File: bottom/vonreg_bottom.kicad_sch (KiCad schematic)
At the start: 7 parts, among them J1 AudioJack4, T1 SW_Push, T2 SW_Push, T3 SW_Push

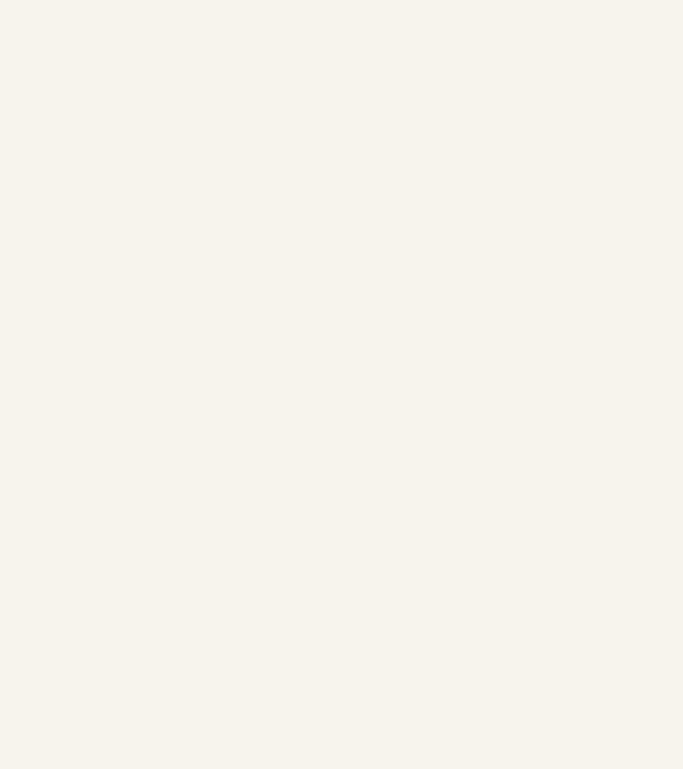
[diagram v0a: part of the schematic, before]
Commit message: Aligned top/bottom
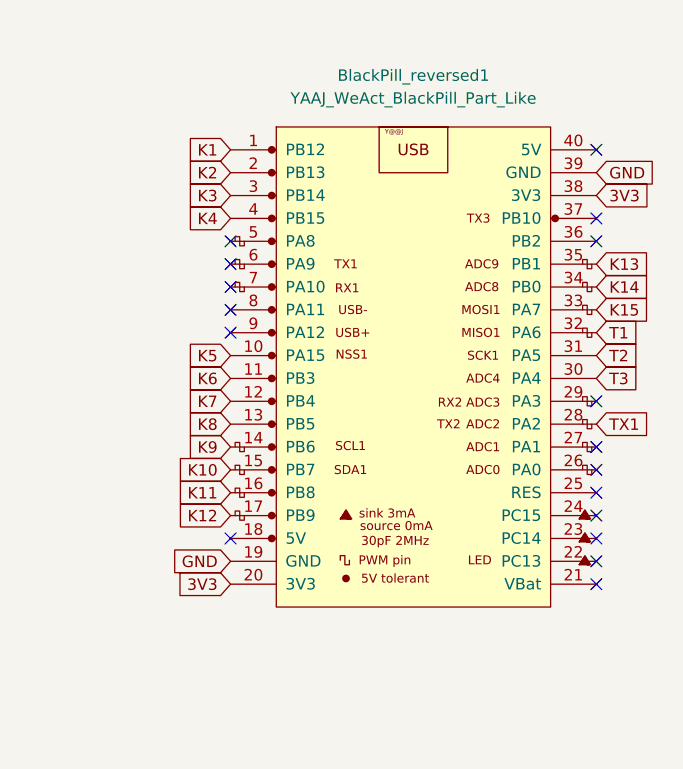
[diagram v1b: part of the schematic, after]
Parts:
- added BlackPill_reversed1: YAAJ_WeAct_BlackPill_Part_Like, Blackpill:YAAJ_WeAct_BlackPill_2, symbol blackpill:YAAJ_WeAct_BlackPill_Part_Like
- BlackPill1: footprint Kicad-STM32:YAAJ_WeAct_BlackPill2 -> Blackpill:YAAJ_WeAct_BlackPill_2
- J1: footprint (none) -> keebio:TRRS-PJ-320A-dual
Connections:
- net 3V3: now also BlackPill_reversed1.20 (3V3), BlackPill_reversed1.38 (3V3)
- net GND: now also BlackPill_reversed1.19 (GND), BlackPill_reversed1.39 (GND)
- net K1: now also BlackPill_reversed1.1 (PB12)
- net K10: now also BlackPill_reversed1.15 (PB7)
- net K11: now also BlackPill_reversed1.16 (PB8)
- net K12: now also BlackPill_reversed1.17 (PB9)
- net K13: now also BlackPill_reversed1.35 (PB1)
- net K14: now also BlackPill_reversed1.34 (PB0)
- net K15: now also BlackPill_reversed1.33 (PA7)
- net K2: now also BlackPill_reversed1.2 (PB13)
- net K3: now also BlackPill_reversed1.3 (PB14)
- net K4: now also BlackPill_reversed1.4 (PB15)
- net K5: now also BlackPill_reversed1.10 (PA15)
- net K6: now also BlackPill_reversed1.11 (PB3)
- net K7: now also BlackPill_reversed1.12 (PB4)
- net K8: now also BlackPill_reversed1.13 (PB5)
- net K9: now also BlackPill_reversed1.14 (PB6)
- net T1: now also BlackPill_reversed1.32 (PA6)
- net T2: now also BlackPill_reversed1.31 (PA5)
- net T3: now also BlackPill_reversed1.30 (PA4)
- net TX1: now also BlackPill_reversed1.28 (PA2)
- no-connect marks 22 -> 39

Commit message: Routing done, hopefully
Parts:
- J1: footprint keebio:TRRS-PJ-320A-dual -> Connector_Audio:TRRS-PJ-320A-dual
- T1, T2, T3: footprint Button_Switch_Keyboard:SW_Cherry_MX_1.00u_PCB -> Button_Switch_Keyboard:Kailh_socket_MX_optional_reversible
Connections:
- net 3V3: no longer BlackPill1.20 (3V3), BlackPill_reversed1.20 (3V3)
- net GND: now also PinsBottomB1.4 (Pin_4); no longer PinsBottomB1.10 (Pin_10)
- net K1: now also BlackPill1.4 (PB15), BlackPill_reversed1.4 (PB15), PinsBottomA1.6 (Pin_6); no longer BlackPill1.1 (PB12), BlackPill_reversed1.1 (PB12), PinsBottomA1.1 (Pin_1)
- net K10: now also BlackPill1.34 (PB0), BlackPill_reversed1.34 (PB0), PinsBottomA1.9 (Pin_9); no longer BlackPill1.15 (PB7), BlackPill_reversed1.15 (PB7), PinsBottomA1.10 (Pin_10)
- net K11: now also BlackPill1.32 (PA6), BlackPill_reversed1.32 (PA6), PinsBottomB1.2 (Pin_2); no longer BlackPill1.16 (PB8), BlackPill_reversed1.16 (PB8), PinsBottomB1.1 (Pin_1)
- net K12: now also BlackPill1.14 (PB6), BlackPill_reversed1.14 (PB6), PinsBottomB1.9 (Pin_9); no longer BlackPill1.17 (PB9), BlackPill_reversed1.17 (PB9), PinsBottomB1.2 (Pin_2)
- net K13: now also BlackPill1.2 (PB13), BlackPill_reversed1.2 (PB13), PinsBottomA1.4 (Pin_4); no longer BlackPill1.35 (PB1), BlackPill_reversed1.35 (PB1), PinsBottomB1.3 (Pin_3)
- net K14: now also BlackPill1.1 (PB12), BlackPill_reversed1.1 (PB12), PinsBottomA1.2 (Pin_2); no longer BlackPill1.34 (PB0), BlackPill_reversed1.34 (PB0), PinsBottomB1.4 (Pin_4)
- net K15: now also BlackPill1.12 (PB4), BlackPill_reversed1.12 (PB4), PinsBottomB1.7 (Pin_7); no longer BlackPill1.33 (PA7), BlackPill_reversed1.33 (PA7), PinsBottomB1.5 (Pin_5)
- net K2: now also BlackPill1.11 (PB3), BlackPill_reversed1.11 (PB3), PinsBottomB1.5 (Pin_5); no longer BlackPill1.2 (PB13), BlackPill_reversed1.2 (PB13), PinsBottomA1.2 (Pin_2)
- net K3: now also BlackPill1.30 (PA4), BlackPill_reversed1.30 (PA4), PinsBottomB1.6 (Pin_6); no longer BlackPill1.3 (PB14), BlackPill_reversed1.3 (PB14), PinsBottomA1.3 (Pin_3)
- net K4: now also BlackPill1.35 (PB1), BlackPill_reversed1.35 (PB1), PinsBottomA1.8 (Pin_8); no longer BlackPill1.4 (PB15), BlackPill_reversed1.4 (PB15), PinsBottomA1.4 (Pin_4)
- net K5: now also PinsBottomB1.3 (Pin_3); no longer PinsBottomA1.5 (Pin_5)
- net K6: now also BlackPill1.28 (PA2), BlackPill_reversed1.28 (PA2), PinsBottomB1.8 (Pin_8); no longer BlackPill1.11 (PB3), BlackPill_reversed1.11 (PB3), PinsBottomA1.6 (Pin_6)
- net K7: now also BlackPill1.33 (PA7), BlackPill_reversed1.33 (PA7), PinsBottomA1.10 (Pin_10); no longer BlackPill1.12 (PB4), BlackPill_reversed1.12 (PB4), PinsBottomA1.7 (Pin_7)
- net K8: now also BlackPill1.31 (PA5), BlackPill_reversed1.31 (PA5), PinsBottomB1.1 (Pin_1); no longer BlackPill1.13 (PB5), BlackPill_reversed1.13 (PB5), PinsBottomA1.8 (Pin_8)
- net K9: now also BlackPill1.13 (PB5), BlackPill_reversed1.13 (PB5), PinsBottomB1.10 (Pin_10); no longer BlackPill1.14 (PB6), BlackPill_reversed1.14 (PB6), PinsBottomA1.9 (Pin_9)
- net T1: now also BlackPill1.17 (PB9), BlackPill_reversed1.17 (PB9); no longer BlackPill1.32 (PA6), BlackPill_reversed1.32 (PA6)
- net T2: now also BlackPill1.16 (PB8), BlackPill_reversed1.16 (PB8); no longer BlackPill1.31 (PA5), BlackPill_reversed1.31 (PA5)
- net T3: now also BlackPill1.15 (PB7), BlackPill_reversed1.15 (PB7); no longer BlackPill1.30 (PA4), BlackPill_reversed1.30 (PA4)
- net TX1: now also BlackPill1.3 (PB14), BlackPill_reversed1.3 (PB14); no longer BlackPill1.28 (PA2), BlackPill_reversed1.28 (PA2)
- no-connect marks 39 -> 41

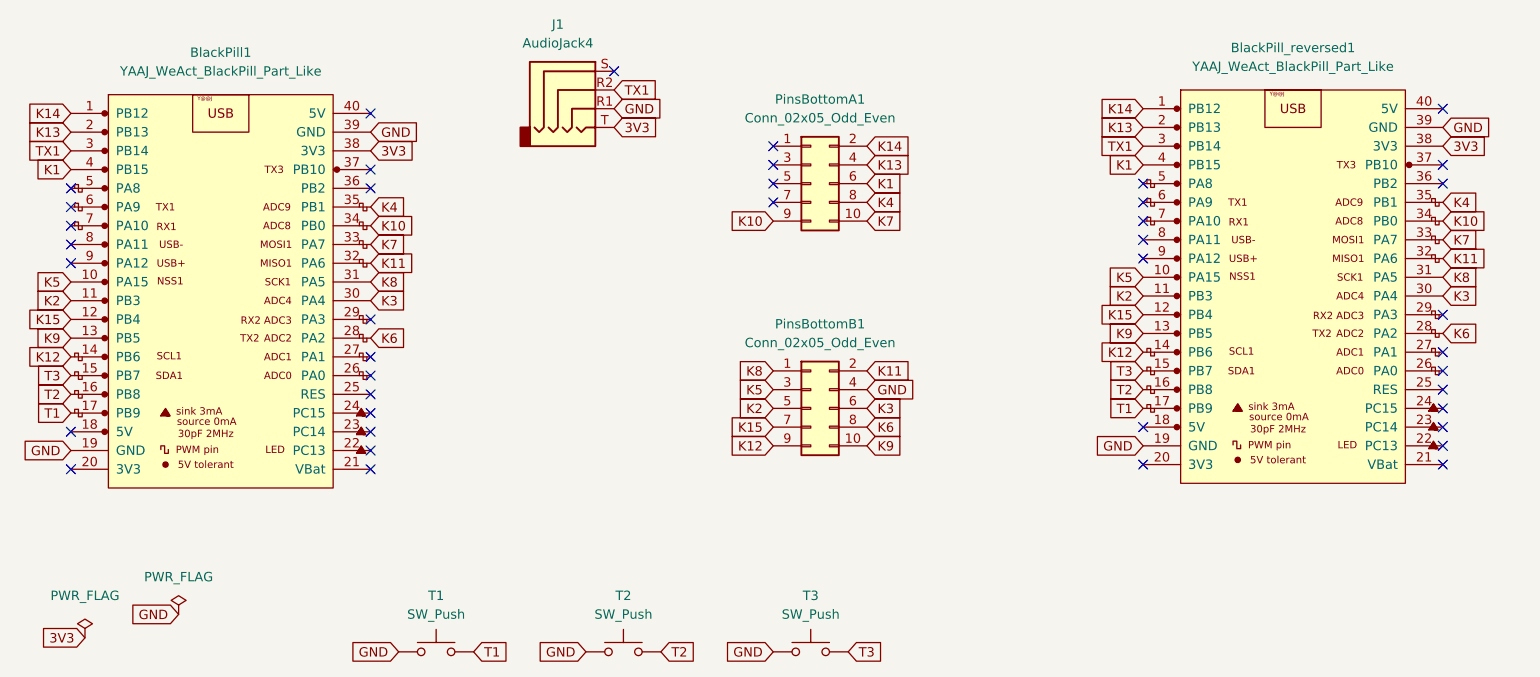
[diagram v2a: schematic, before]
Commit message: Ground pour and buzzer
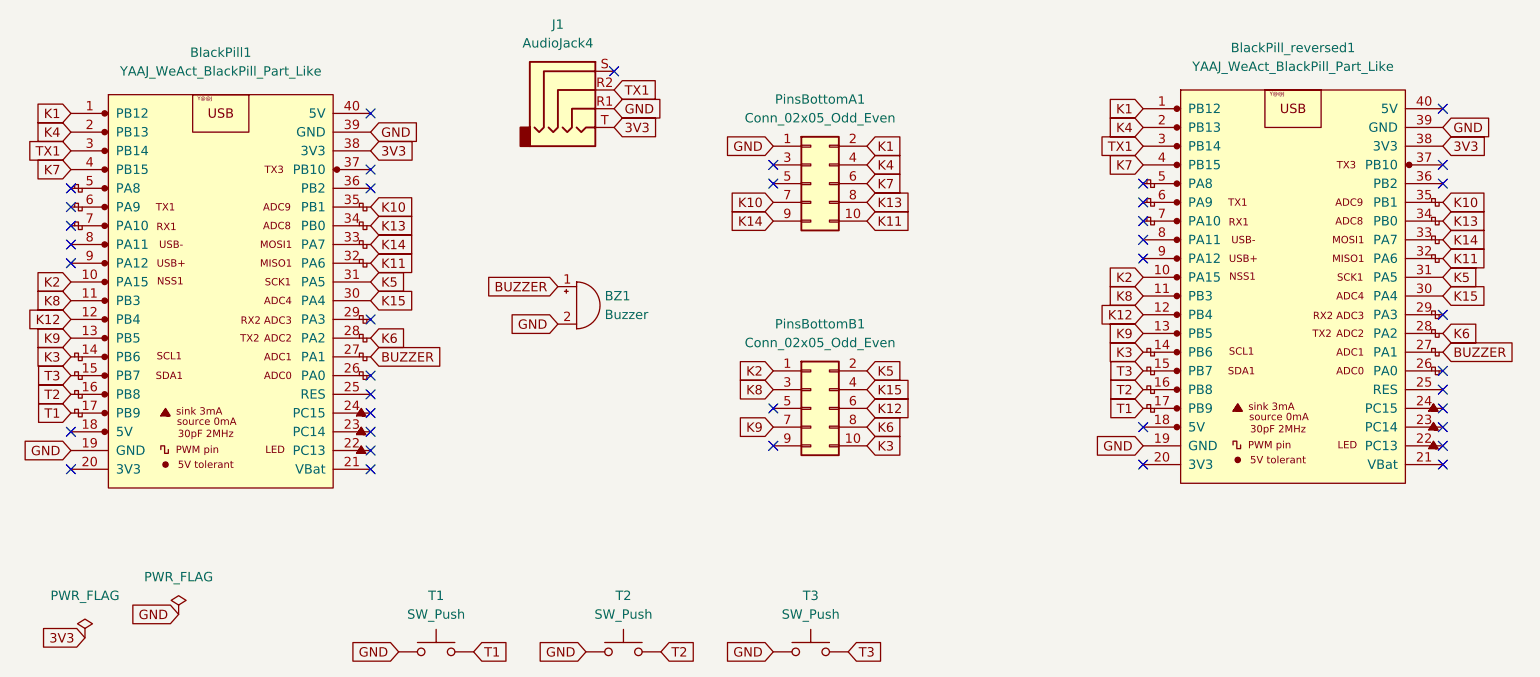
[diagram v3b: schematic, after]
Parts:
- added BZ1: Buzzer, Buzzer_Beeper:MagneticBuzzer_PUI_AT-0927-TT-6-R, symbol Device:Buzzer
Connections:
- net GND: now also PinsBottomA1.1 (Pin_1), BZ1.2 (+); no longer PinsBottomB1.4 (Pin_4)
- net K1: now also BlackPill1.1 (PB12), BlackPill_reversed1.1 (PB12), PinsBottomA1.2 (Pin_2); no longer BlackPill1.4 (PB15), BlackPill_reversed1.4 (PB15), PinsBottomA1.6 (Pin_6)
- net K10: now also BlackPill1.35 (PB1), BlackPill_reversed1.35 (PB1), PinsBottomA1.7 (Pin_7); no longer BlackPill1.34 (PB0), BlackPill_reversed1.34 (PB0), PinsBottomA1.9 (Pin_9)
- net K11: now also PinsBottomA1.10 (Pin_10); no longer PinsBottomB1.2 (Pin_2)
- net K12: now also BlackPill1.12 (PB4), BlackPill_reversed1.12 (PB4), PinsBottomB1.6 (Pin_6); no longer BlackPill1.14 (PB6), BlackPill_reversed1.14 (PB6), PinsBottomB1.9 (Pin_9)
- net K13: now also BlackPill1.34 (PB0), BlackPill_reversed1.34 (PB0), PinsBottomA1.8 (Pin_8); no longer BlackPill1.2 (PB13), BlackPill_reversed1.2 (PB13), PinsBottomA1.4 (Pin_4)
- net K14: now also BlackPill1.33 (PA7), BlackPill_reversed1.33 (PA7), PinsBottomA1.9 (Pin_9); no longer BlackPill1.1 (PB12), BlackPill_reversed1.1 (PB12), PinsBottomA1.2 (Pin_2)
- net K15: now also BlackPill1.30 (PA4), BlackPill_reversed1.30 (PA4), PinsBottomB1.4 (Pin_4); no longer BlackPill1.12 (PB4), BlackPill_reversed1.12 (PB4), PinsBottomB1.7 (Pin_7)
- net K2: now also BlackPill1.10 (PA15), BlackPill_reversed1.10 (PA15), PinsBottomB1.1 (Pin_1); no longer BlackPill1.11 (PB3), BlackPill_reversed1.11 (PB3), PinsBottomB1.5 (Pin_5)
- net K3: now also BlackPill1.14 (PB6), BlackPill_reversed1.14 (PB6), PinsBottomB1.10 (Pin_10); no longer BlackPill1.30 (PA4), BlackPill_reversed1.30 (PA4), PinsBottomB1.6 (Pin_6)
- net K4: now also BlackPill1.2 (PB13), BlackPill_reversed1.2 (PB13), PinsBottomA1.4 (Pin_4); no longer BlackPill1.35 (PB1), BlackPill_reversed1.35 (PB1), PinsBottomA1.8 (Pin_8)
- net K5: now also BlackPill1.31 (PA5), BlackPill_reversed1.31 (PA5), PinsBottomB1.2 (Pin_2); no longer BlackPill1.10 (PA15), BlackPill_reversed1.10 (PA15), PinsBottomB1.3 (Pin_3)
- net K7: now also BlackPill1.4 (PB15), BlackPill_reversed1.4 (PB15), PinsBottomA1.6 (Pin_6); no longer BlackPill1.33 (PA7), BlackPill_reversed1.33 (PA7), PinsBottomA1.10 (Pin_10)
- net K8: now also BlackPill1.11 (PB3), BlackPill_reversed1.11 (PB3), PinsBottomB1.3 (Pin_3); no longer BlackPill1.31 (PA5), BlackPill_reversed1.31 (PA5), PinsBottomB1.1 (Pin_1)
- net K9: now also PinsBottomB1.7 (Pin_7); no longer PinsBottomB1.10 (Pin_10)
- net BUZZER: now reaches BlackPill_reversed1.27 (PA1)
- net BUZZER: now also BlackPill1.27 (PA1), BZ1.1 (-)
- no-connect marks 41 -> 39
